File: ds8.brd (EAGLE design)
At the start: 85 x 50 mm, 87 parts, among them IC1 TM4C1230C3PM, IC2 TPS77333, Q1 BC850, Q2 BC850, Q3 BC850, U1 LM13700M, U2 LM324, U3 LM324, U4 LM741D

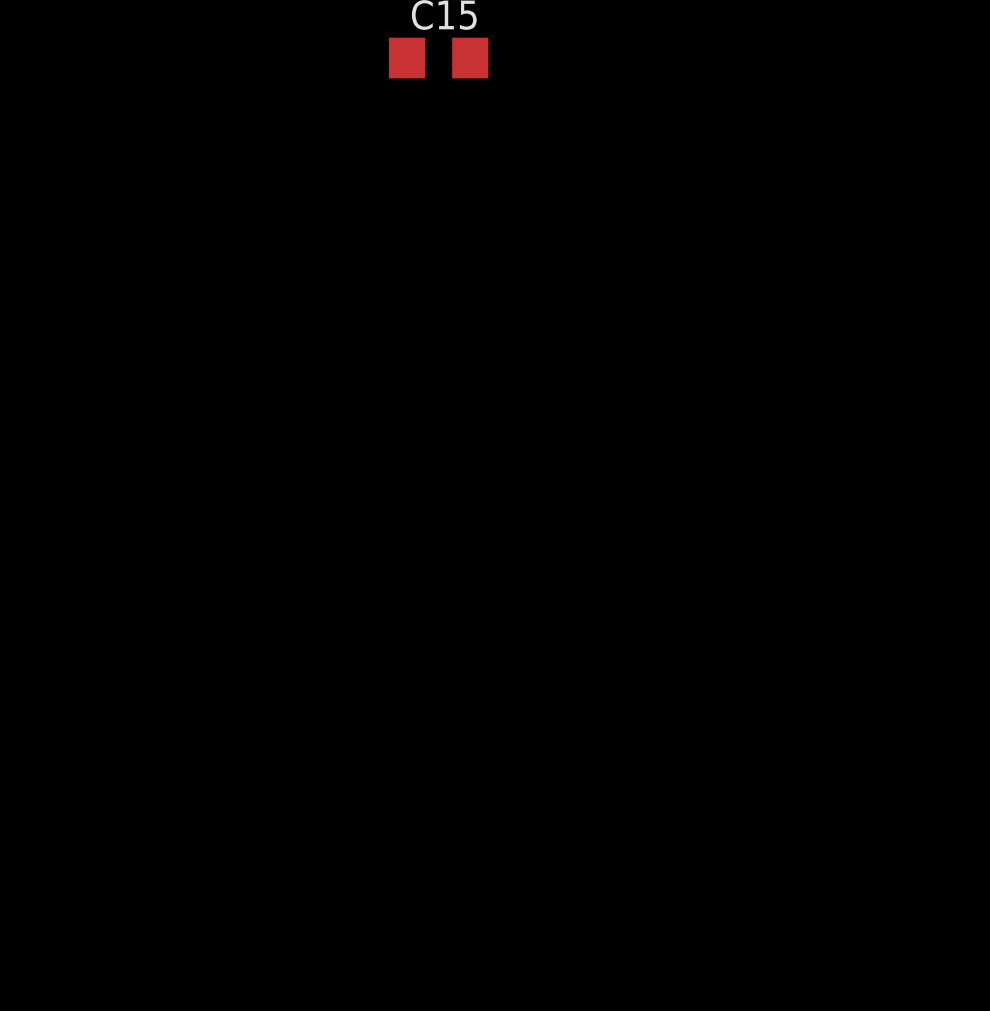
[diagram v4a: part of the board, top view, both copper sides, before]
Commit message: added optocoupler
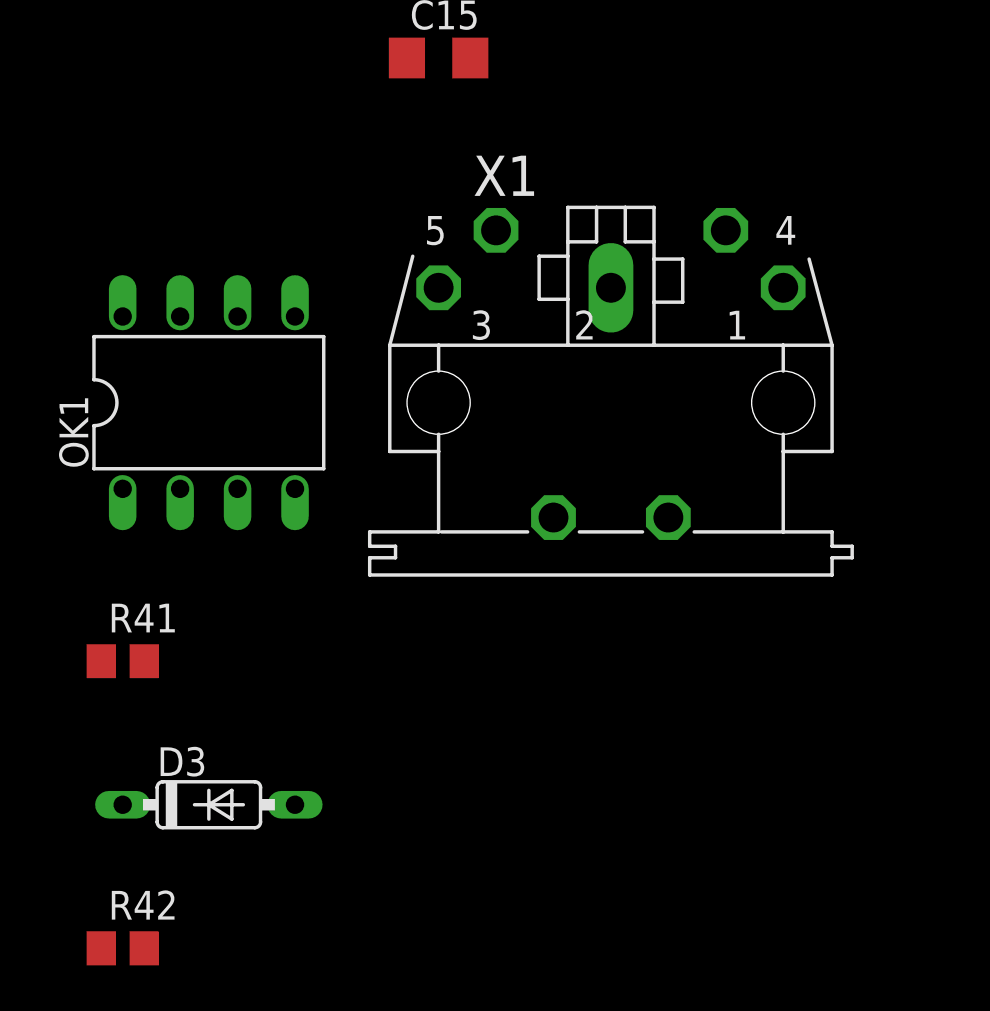
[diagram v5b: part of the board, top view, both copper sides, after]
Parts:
- added D3: 1N4148DO35-7, diode:DO35-7
- added OK1: 6N138, optocoupler:DIL08
- added R41, R42: 220, rcl:R0805
- added X1: MAB5SH, con-hirschmann:MAB5SH
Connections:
- new net MIDI_IN: IC1.17, OK1.6, R42.1
- new net N$18: R41.1, X1.4
- new net N$26: D3.C, OK1.2, R41.2
- new net N$35: D3.A, OK1.3, X1.5
- new net PE: X1.PE, X1.PE@
- net GND: now also OK1.5
- net VCC: now also OK1.8, R42.2
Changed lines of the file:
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@@
 <element name="U$1" library="ds8" package="SOT-23-6" value="DAC7512" x="-15.24" y="-41.91"/>
 <element name="C15" library="rcl" package="C1206" value="3uF" x="-13.97" y="-48.26"/>
+<element name="X1" library="con-hirschmann" package="MAB5SH" value="MAB5SH" x="-6.35" y="-63.5">
+<attribute name="OC_NEWARK" value="unknown" x="-6.35" y="-63.5" size="1.778" layer="27" display="off"/>
+<attribute name="MPN" value="" x="-6.35" y="-63.5" size="1.778" layer="27" display="off"/>
+<attribute name="MF" value="" x="-6.35" y="-63.5" size="1.778" layer="27" display="off"/>
+<attribute name="OC_FARNELL" value="809883" x="-6.35" y="-63.5" size="1.778" layer="27" display="off"/>
+</element>
+<element name="OK1" library="optocoupler" package="DIL08" value="6N138" x="-24.13" y="-63.5">
+<attribute name="OC_NEWARK" value="35K5294" x="-24.13" y="-63.5" size="1.778" layer="27" display="off"/>
+<attribute name="MPN" value="6N138" x="-24.13" y="-63.5" size="1.778" layer="27" display="off"/>
+<attribute name="MF" value="VISHAY/TELEFUNKEN" x="-24.13" y="-63.5" size="1.778" layer="27" display="off"/>
+<attribute name="OC_FARNELL" value="9860150" x="-24.13" y="-63.5" size="1.778" layer="27" display="off"/>
+</element>
+<element name="R41" library="rcl" package="R0805" value="220" x="-27.94" y="-74.93"/>
+<element name="D3" library="diode" package="DO35-7" value="1N4148DO35-7" x="-24.13" y="-81.28"/>
+<element name="R42" library="rcl" package="R0805" value="220" x="-27.94" y="-87.63"/>
 </elements>
 <signals>
@@
 <contactref element="IC1" pad="39"/>
 <contactref element="IC1" pad="27"/>
+<contactref element="OK1" pad="5"/>
 <wire x1="56.69" y1="34.655" x2="69.39" y2="47.26" width="0" layer="19" extent="1-1"/>
 <wire x1="56.69" y1="32.02" x2="56.69" y2="34.655" width="0" layer="19" extent="1-1"/>
@@
 <wire x1="-15.24" y1="-43.06" x2="-15.37" y2="-35.56" width="0" layer="19" extent="1-1"/>
 <wire x1="-15.37" y1="-48.26" x2="-15.24" y2="-43.06" width="0" layer="19" extent="1-1"/>
+<wire x1="-20.32" y1="-59.69" x2="-15.37" y2="-48.26" width="0" layer="19" extent="1-1"/>
 <wire x1="82.09" y1="28.21" x2="63.675" y2="28.33" width="0" layer="19" extent="1-1"/>
 </signal>
@@
 <wire x1="71.93" y1="14.24" x2="71.93" y2="15.83" width="0.6096" layer="1"/>
 <contactref element="U$1" pad="3"/>
-<wire x1="54.785" y1="26.94" x2="54.9247" y2="26.94" width="0" layer="19" extent="1-1"/>
-<wire x1="22.34" y1="13.605" x2="23.67" y2="13.605" width="0" layer="19" extent="1-1"/>
-<wire x1="56.055" y1="5.4516" x2="56.055" y2="4.08" width="0" layer="19" extent="1-1"/>
-<wire x1="16.05" y1="17.32" x2="18.05" y2="17.32" width="0" layer="19" extent="1-1"/>
-<wire x1="43.99" y1="28.625" x2="44.625" y2="30.75" width="0" layer="19" extent="1-1"/>
-<wire x1="13.795" y1="17.32" x2="16.05" y2="17.32" width="0" layer="19" extent="1-1"/>
+<contactref element="R42" pad="2"/>
+<contactref element="OK1" pad="8"/>
+<wire x1="-27.94" y1="-59.69" x2="-26.99" y2="-87.63" width="0" layer="19" extent="1-1"/>
+<wire x1="-14.29" y1="-43.06" x2="-27.94" y2="-59.69" width="0" layer="19" extent="1-1"/>
+<wire x1="-12.57" y1="-16.51" x2="-14.29" y2="-43.06" width="0" layer="19" extent="1-1"/>
+<wire x1="-10.795" y1="-4.045" x2="-12.57" y2="-16.51" width="0" layer="19" extent="1-1"/>
+<wire x1="-9.525" y1="-4.045" x2="-10.795" y2="-4.045" width="0" layer="19" extent="1-1"/>
+<wire x1="4.66" y1="2.85" x2="-9.525" y2="-4.045" width="0" layer="19" extent="1-1"/>
+<wire x1="9.105" y1="2.85" x2="4.66" y2="2.85" width="0" layer="19" extent="1-1"/>
 <wire x1="8.43" y1="22.18" x2="9.065" y2="22.18" width="0" layer="19" extent="1-1"/>
 <wire x1="18.59" y1="41.23" x2="17.005" y2="41.23" width="0" layer="19" extent="1-1"/>
-<wire x1="4.66" y1="2.85" x2="9.105" y2="2.85" width="0" layer="19" extent="1-1"/>
-<wire x1="-9.525" y1="-4.045" x2="4.66" y2="2.85" width="0" layer="19" extent="1-1"/>
-<wire x1="-10.795" y1="-4.045" x2="-9.525" y2="-4.045" width="0" layer="19" extent="1-1"/>
-<wire x1="-12.57" y1="-16.51" x2="-10.795" y2="-4.045" width="0" layer="19" extent="1-1"/>
-<wire x1="-14.29" y1="-43.06" x2="-12.57" y2="-16.51" width="0" layer="19" extent="1-1"/>
+<wire x1="16.05" y1="17.32" x2="13.795" y2="17.32" width="0" layer="19" extent="1-1"/>
+<wire x1="18.05" y1="17.32" x2="16.05" y2="17.32" width="0" layer="19" extent="1-1"/>
+<wire x1="23.67" y1="13.605" x2="22.34" y2="13.605" width="0" layer="19" extent="1-1"/>
+<wire x1="54.9247" y1="26.94" x2="54.785" y2="26.94" width="0" layer="19" extent="1-1"/>
+<wire x1="56.055" y1="5.4516" x2="56.055" y2="4.08" width="0" layer="19" extent="1-1"/>
+<wire x1="43.99" y1="28.625" x2="44.625" y2="30.75" width="0" layer="19" extent="1-1"/>
 </signal>
 <signal name="N$5">
@@
 <wire x1="-9.835" y1="14.67" x2="-12.57" y2="-48.26" width="0" layer="19" extent="1-1"/>
 </signal>
+<signal name="PE">
+<contactref element="X1" pad="PE"/>
+<contactref element="X1" pad="PE@"/>
+<wire x1="-3.81" y1="-68.58" x2="-8.89" y2="-68.58" width="0" layer="19" extent="1-1"/>
+</signal>
+<signal name="N$18">
+<contactref element="X1" pad="4"/>
+<contactref element="R41" pad="1"/>
+<wire x1="-1.27" y1="-55.88" x2="-28.89" y2="-74.93" width="0" layer="19" extent="1-1"/>
+</signal>
+<signal name="N$26">
+<contactref element="R41" pad="2"/>
+<contactref element="OK1" pad="2"/>
+<contactref element="D3" pad="C"/>
+<wire x1="-26.99" y1="-74.93" x2="-27.94" y2="-81.28" width="0" layer="19" extent="1-1"/>
+<wire x1="-25.4" y1="-67.31" x2="-26.99" y2="-74.93" width="0" layer="19" extent="1-1"/>
+</signal>
+<signal name="N$35">
+<contactref element="OK1" pad="3"/>
+<contactref element="X1" pad="5"/>
+<contactref element="D3" pad="A"/>
+<wire x1="-22.86" y1="-67.31" x2="-20.32" y2="-81.28" width="0" layer="19" extent="1-1"/>
+<wire x1="-11.43" y1="-55.88" x2="-22.86" y2="-67.31" width="0" layer="19" extent="1-1"/>
+</signal>
+<signal name="MIDI_IN">
+<contactref element="OK1" pad="6"/>
+<contactref element="R42" pad="1"/>
+<contactref element="IC1" pad="17"/>
+<wire x1="-22.86" y1="-59.69" x2="-28.89" y2="-87.63" width="0" layer="19" extent="1-1"/>
+<wire x1="-15.035" y1="0.57" x2="-22.86" y2="-59.69" width="0" layer="19" extent="1-1"/>
+</signal>
 </signals>

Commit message: added SW debug on midi connector
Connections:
- new net SWCLK: IC1.52, X1.1
- new net SWDIO: IC1.51, X1.3
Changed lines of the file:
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@@
 <wire x1="-15.035" y1="0.57" x2="-22.86" y2="-59.69" width="0" layer="19" extent="1-1"/>
+</signal>
+<signal name="SWCLK">
+<contactref element="IC1" pad="52"/>
+<contactref element="X1" pad="1"/>
+<wire x1="-7.235" y1="14.67" x2="1.27" y2="-58.42" width="0" layer="19" extent="1-1"/>
+</signal>
+<signal name="SWDIO">
+<contactref element="IC1" pad="51"/>
+<contactref element="X1" pad="3"/>
+<wire x1="-6.585" y1="14.67" x2="-13.97" y2="-58.42" width="0" layer="19" extent="1-1"/>
 </signal>
 </signals>
